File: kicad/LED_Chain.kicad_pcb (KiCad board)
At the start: 2 copper layers, 66.7 x 31.5 mm, 32 parts, among them J1 Interface, J2 PWR, J3 NeoPixel R1 A, J4 NeoPixel R1 B, J5 NeoPixel R1 C, J6 NeoPixel R1 D, J7 L1, J8 L2, Q1 IRLML2502, Q2 IRLML2502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

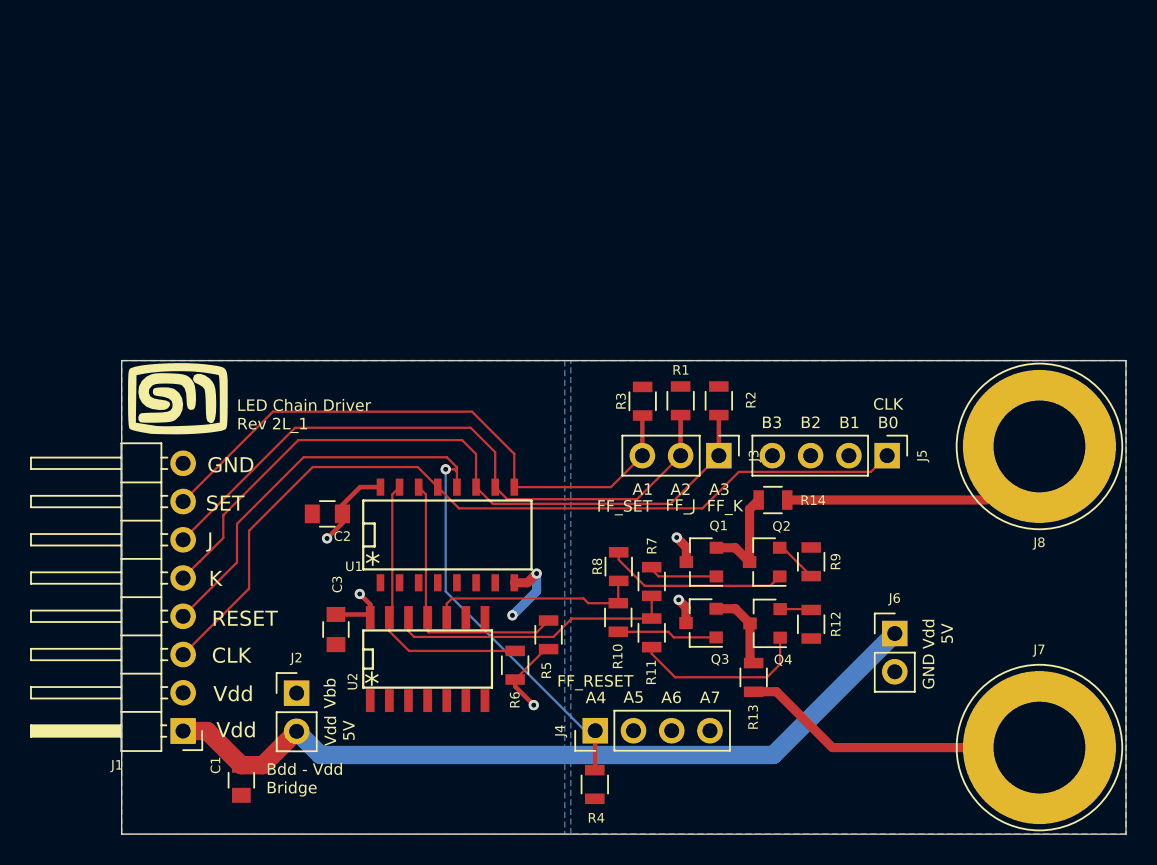
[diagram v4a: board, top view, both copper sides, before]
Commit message: Completed layout and sent to OSH Park
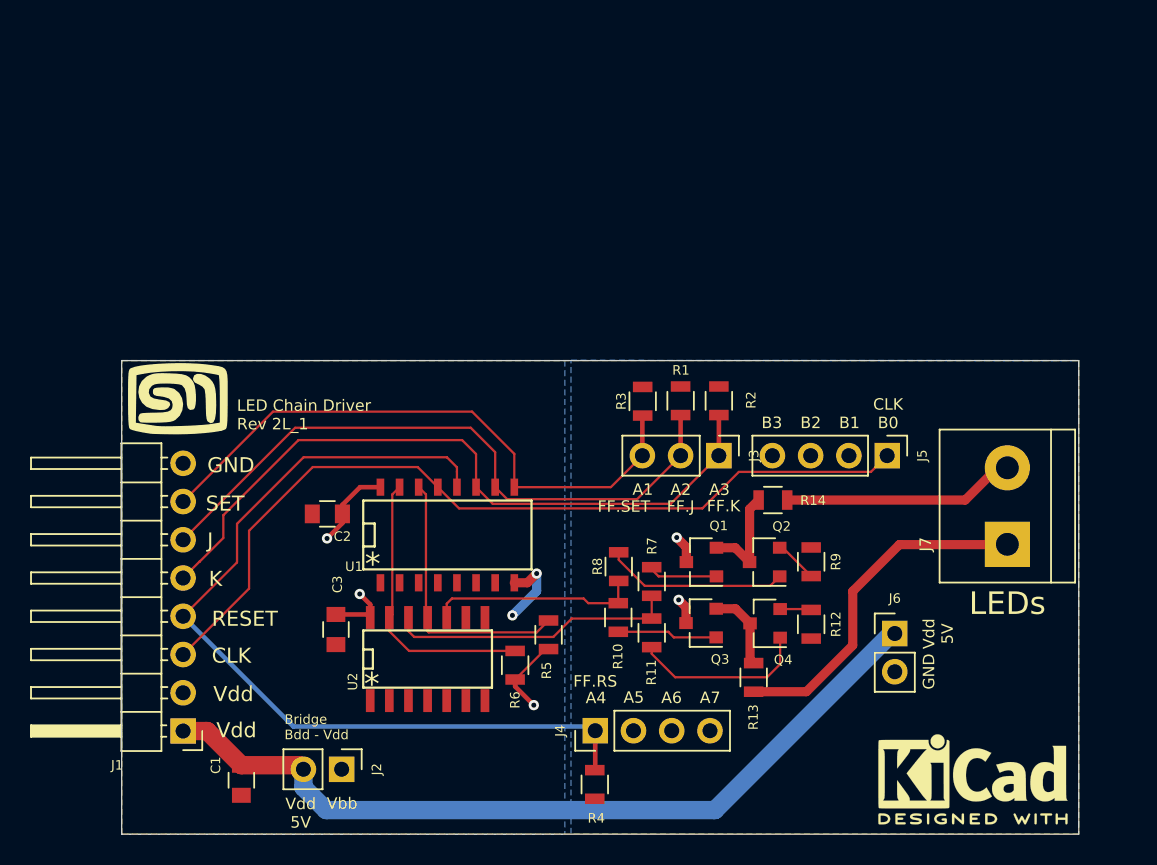
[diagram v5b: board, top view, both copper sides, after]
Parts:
- removed J8: L2, Connect:Banana_Jack_1Pin
- added G***: LOGO, LED_Chain:MyBasic_rounded_50_1, B.Cu at (149.7, 94.3)
- added REF***: KiCad-Logo2_6mm_SilkScreen, Symbols:KiCad-Logo2_6mm_SilkScreen, B.Cu at (173.1, 107.8)
- added REF***: KiCad-Logo2_6mm_SilkScreen, Symbols:KiCad-Logo2_6mm_SilkScreen, F.Cu at (173.1, 107.7)
- J7: value L1 -> LED; footprint Connect:Banana_Jack_1Pin -> LED_Chain:TerminalBlock_bornier-2_P5.08mm
- moved J7 13.7 mm to (175.4, 92.1), turned to 90 degrees
- moved J2 5.88 mm to (131.2, 107.1), turned to 270 degrees
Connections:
- net Net-(J7-Pad1) renamed /LED1
- R14 pad 1: Net-(J8-Pad1) -> /LED2
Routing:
- net Net-(J8-Pad1): track 18.2 -> 0.00 mm
- net /LED2: track 0.00 -> 14.8 mm
- net /A4: track 51.0 -> 58.8 mm, vias 1 -> 0
- net /5V: track 56.8 -> 58.9 mm
- net /LED1: track 21.7 -> 23.5 mm
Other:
- board size 66.7 x 31.5 mm -> 63.6 x 31.5 mm
- board text added: "Bridge Bdd - Vdd"
- board text added: "FF.J"
- board text added: "FF.K"
- board text added: "FF.RS"
- board text added: "FF.SET"
- board text added: "LEDs"
- board text removed: "B0 CLK"
- board text removed: "Bdd - Vdd Bridge"
- board text removed: "FF_J"
- board text removed: "FF_K"
- board text removed: "FF_RESET"
- board text removed: "FF_SET"

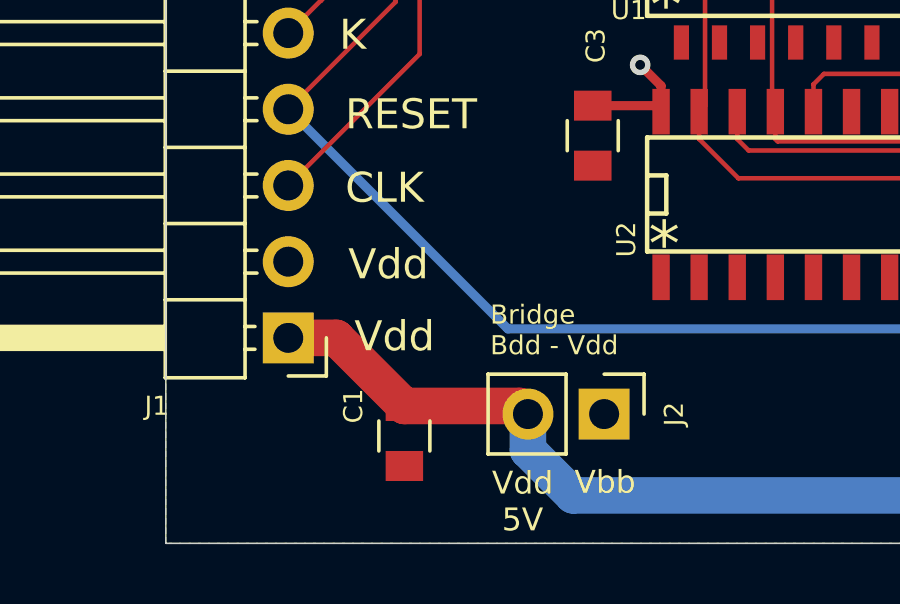
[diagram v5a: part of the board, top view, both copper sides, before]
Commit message: Makes a small correction to the labelling of the Vbb-Vdd bridge
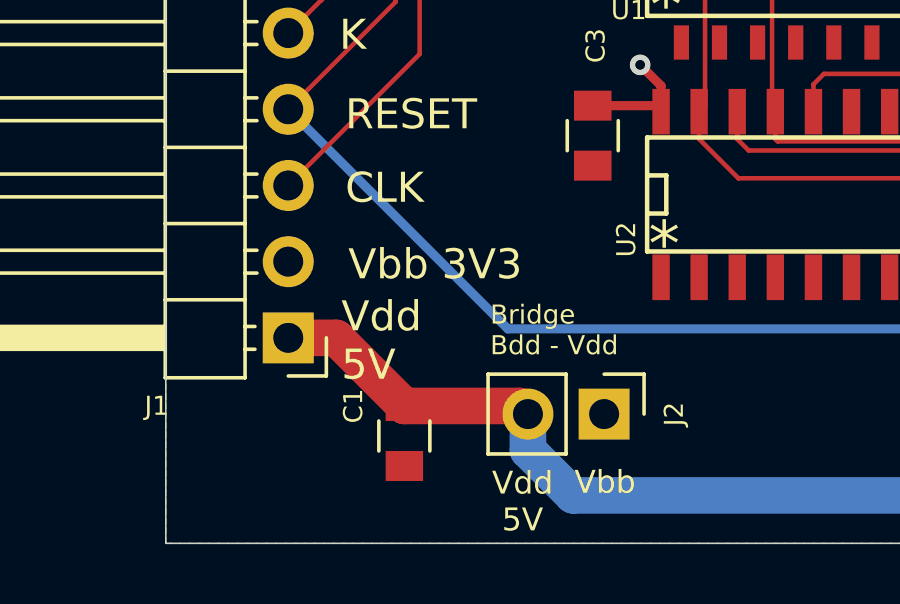
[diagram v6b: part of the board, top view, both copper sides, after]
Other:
- board text added: "Vbb 3V3"
- board text removed: "Vdd"
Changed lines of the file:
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@@
   )
   (setup
-    (last_trace_width 0.3048)
+    (last_trace_width 0.1524)
     (user_trace_width 0.3048)
     (user_trace_width 0.6096)
@@
       (effects (font (size 1 1) (thickness 0.15)))
     )
-    (fp_text user %R (at 2.54 0 90) (layer F.Fab)
-      (effects (font (size 1 1) (thickness 0.15)))
-    )
     (fp_line (start -2.41 2.85) (end 7.49 2.85) (layer F.Fab) (width 0.1))
     (fp_line (start -2.46 -4.45) (end -2.46 4.45) (layer F.Fab) (width 0.1))
@@
     (fp_line (start 7.79 4.7) (end 7.79 -4.7) (layer F.CrtYd) (width 0.05))
     (fp_line (start 7.79 4.7) (end -2.71 4.7) (layer F.CrtYd) (width 0.05))
+    (fp_text user %R (at 2.54 0 90) (layer F.Fab)
+      (effects (font (size 1 1) (thickness 0.15)))
+    )
     (pad 1 thru_hole rect (at 0 0 90) (size 3 3) (drill 1.52) (layers *.Cu *.Mask)
       (net 21 /LED1))
@@
   (gr_line (start 157.37 106.34) (end 107.61 106.34) (layer Dwgs.User) (width 0.15))
   (gr_line (start 149.36 80.62) (end 149.36 110.62) (layer Dwgs.User) (width 0.15))
-  (gr_text Vdd (at 125.513333 104.47) (layer F.SilkS)
-    (effects (font (size 1 1) (thickness 0.15)) (justify right))
-  )
-  (gr_text Vdd (at 122.660951 104.470001) (layer B.SilkS)
+  (gr_text "Vdd \n5V" (at 122.4 104.61) (layer F.SilkS)
+    (effects (font (size 1 1) (thickness 0.15)) (justify left))
+  )
+  (gr_text "Vdd 5V" (at 122.660951 104.470001) (layer B.SilkS)
     (effects (font (size 1 1) (thickness 0.15)) (justify right mirror))
   )
@@
     (effects (font (size 1 1) (thickness 0.15)) (justify right mirror))
   )
-  (gr_text Vdd (at 122.66095 102.070001) (layer B.SilkS)
+  (gr_text "Vbb 3V3" (at 122.66095 102.070001) (layer B.SilkS)
     (effects (font (size 1 1) (thickness 0.15)) (justify right mirror))
   )
-  (gr_text Vdd (at 122.63 102.07) (layer F.SilkS)
+  (gr_text "Vbb 3V3" (at 122.63 102.07) (layer F.SilkS)
     (effects (font (size 1 1) (thickness 0.15)) (justify left))
   )
@@
   (segment (start 134.326999 97.892399) (end 135.6346 99.2) (width 0.1524) (layer F.Cu) (net 14))
   (segment (start 134.326999 96.979999) (end 134.326999 97.892399) (width 0.1524) (layer F.Cu) (net 14))
-  (segment (start 158.52 101.91) (end 159.67 101.91) (width 0.1524) (layer F.Cu) (net 21))
   (via (at 153.54 95.81) (size 0.6858) (drill 0.3302) (layers F.Cu B.Cu) (net 15))
   (segment (start 154.03 96.3) (end 153.54 95.81) (width 0.6096) (layer F.Cu) (net 15))
@@
   (segment (start 140.084999 86.124999) (end 140.084999 88.324998) (width 0.1524) (layer F.Cu) (net 20))
   (segment (start 139.16 85.2) (end 140.084999 86.124999) (width 0.1524) (layer F.Cu) (net 20))
+  (segment (start 158.52 101.91) (end 159.67 101.91) (width 0.1524) (layer F.Cu) (net 21))
   (segment (start 168.2 92.14) (end 174.69 92.14) (width 0.6096) (layer F.Cu) (net 21))
   (segment (start 165.1 95.24) (end 168.2 92.14) (width 0.6096) (layer F.Cu) (net 21))

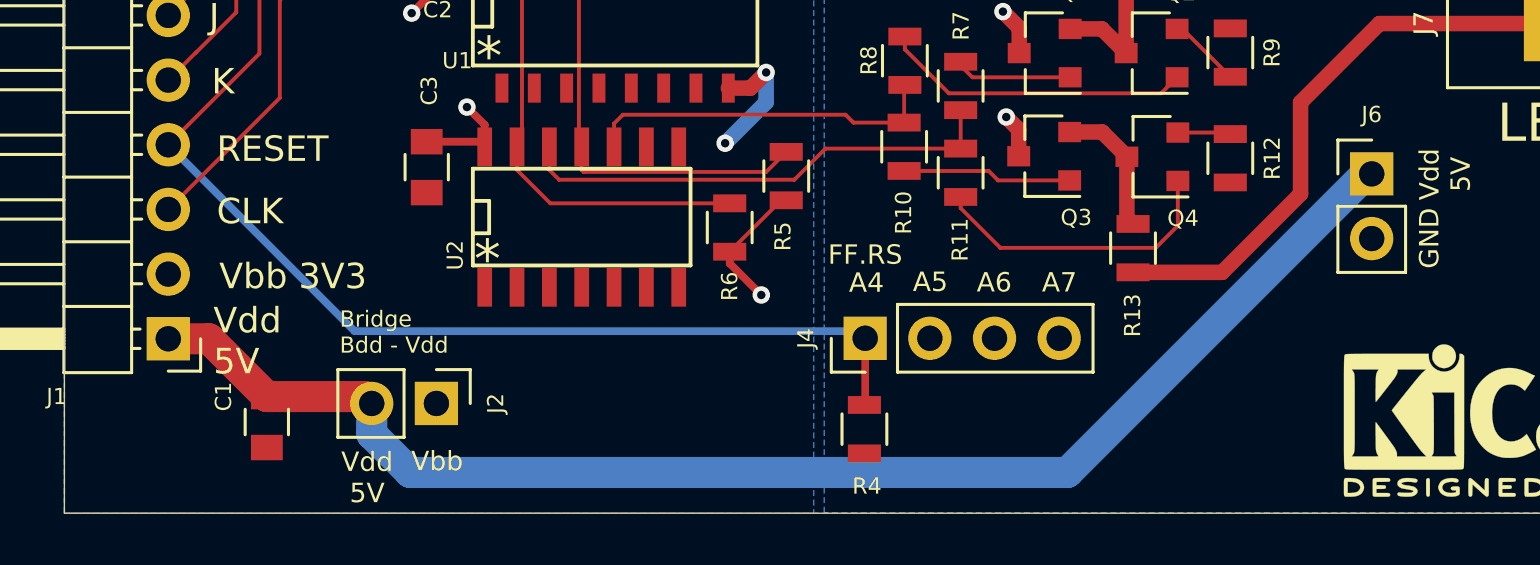
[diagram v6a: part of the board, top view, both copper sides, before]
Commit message: Makes a small correction to the labelling of the Vbb-Vdd bridge
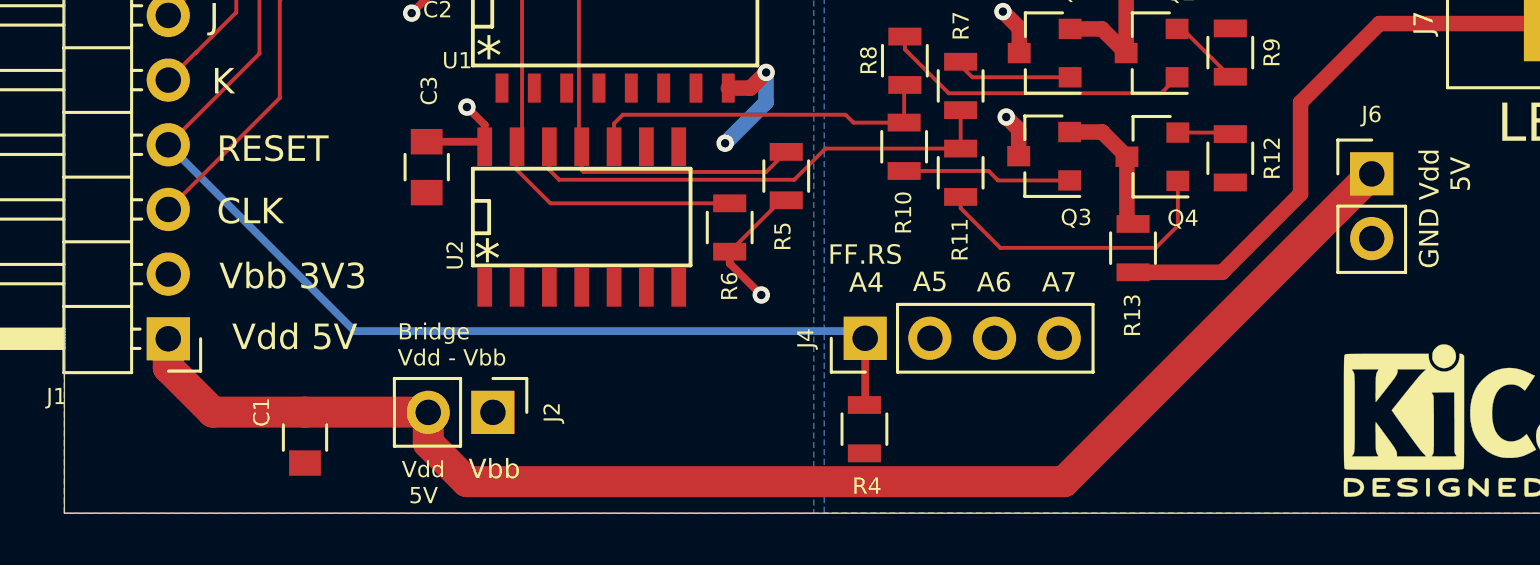
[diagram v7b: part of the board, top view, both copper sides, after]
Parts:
- moved J2 2.25 mm to (133.4, 107.4)
- moved C1 1.62 mm to (126.0, 108.4)
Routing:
- net /5V: track 58.9 -> 59.6 mm
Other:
- board text added: "Bridge Vdd - Vbb"
- board text removed: "Bridge Bdd - Vdd"
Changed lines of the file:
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@@
   )
   (setup
-    (last_trace_width 0.1524)
+    (last_trace_width 1.2192)
     (user_trace_width 0.3048)
     (user_trace_width 0.6096)
@@
   )
   (module Pin_Headers:Pin_Header_Straight_1x02_Pitch2.54mm (layer F.Cu)
-    (at 131.16 107.06 270)
+    (at 133.38 107.41 270)
     (descr "Through hole straight pin header, 1x02, 2.54mm pitch, single row")
     (tags "Through hole pin header THT 1x02 2.54mm single row")
@@
   )
   (module Capacitors_SMD:C_0805 (layer F.Cu)
-    (at 124.5 107.79 270)
+    (at 126 108.4 270)
     (descr "Capacitor SMD 0805, reflow soldering, AVX (see smccp.pdf)")
     (tags "capacitor 0805")
@@
     (effects (font (size 1.524 1.524) (thickness 0.127)) (justify left))
   )
-  (gr_text Vbb (at 131.19 109.33) (layer F.SilkS)
+  (gr_text Vbb (at 133.44 109.64) (layer F.SilkS)
     (effects (font (size 0.762 0.762) (thickness 0.127)))
   )
-  (gr_text "Vdd\n5V" (at 128.44 109.97) (layer F.SilkS)
-    (effects (font (size 0.762 0.762) (thickness 0.127)))
+  (gr_text "Vdd\n5V" (at 130.65 110.17) (layer F.SilkS)
+    (effects (font (size 0.635 0.635) (thickness 0.127)))
   )
   (gr_text FF.K (at 155.41 89.58) (layer F.SilkS)
@@
     (effects (font (size 0.762 0.762) (thickness 0.127)))
   )
-  (gr_text "Bridge\nBdd - Vdd" (at 127.36 104.26) (layer F.SilkS)
+  (gr_text "Bridge\nVdd - Vbb" (at 129.64 104.76) (layer F.SilkS)
     (effects (font (size 0.635 0.635) (thickness 0.127)) (justify left))
   )
@@
   (gr_line (start 157.37 106.34) (end 107.61 106.34) (layer Dwgs.User) (width 0.15))
   (gr_line (start 149.36 80.62) (end 149.36 110.62) (layer Dwgs.User) (width 0.15))
-  (gr_text "Vdd \n5V" (at 122.4 104.61) (layer F.SilkS)
-    (effects (font (size 1 1) (thickness 0.15)) (justify left))
+  (gr_text "Vdd 5V" (at 128.06 104.46) (layer F.SilkS)
+    (effects (font (size 1 1) (thickness 0.15)) (justify right))
   )
   (gr_text "Vdd 5V" (at 122.660951 104.470001) (layer B.SilkS)
@@
   (segment (start 154.049999 92.309999) (end 153.41 91.67) (width 0.6096) (layer F.Cu) (net 15))
   (segment (start 154.049999 93.299999) (end 154.049999 92.309999) (width 0.6096) (layer F.Cu) (net 15))
-  (segment (start 122.23 104.52) (end 124.5 106.79) (width 1.2192) (layer F.Cu) (net 15))
-  (segment (start 120.63 104.52) (end 122.23 104.52) (width 1.2192) (layer F.Cu) (net 15))
-  (segment (start 128.35 106.79) (end 128.62 107.06) (width 1.2192) (layer F.Cu) (net 15))
-  (segment (start 124.5 106.79) (end 128.35 106.79) (width 1.2192) (layer F.Cu) (net 15))
-  (segment (start 167.894 98.044) (end 167.894 97.824) (width 1.2192) (layer B.Cu) (net 15))
-  (segment (start 167.894 97.824) (end 155.948 109.77) (width 1.2192) (layer B.Cu) (net 15))
-  (segment (start 128.62 108.262081) (end 128.62 107.06) (width 1.2192) (layer B.Cu) (net 15))
-  (segment (start 130.127919 109.77) (end 128.62 108.262081) (width 1.2192) (layer B.Cu) (net 15))
-  (segment (start 155.948 109.77) (end 130.127919 109.77) (width 1.2192) (layer B.Cu) (net 15))
+  (segment (start 120.63 104.52) (end 120.63 105.65) (width 1.2192) (layer F.Cu) (net 15))
+  (segment (start 122.38 107.4) (end 126 107.4) (width 1.2192) (layer F.Cu) (net 15))
+  (segment (start 120.63 105.65) (end 122.38 107.4) (width 1.2192) (layer F.Cu) (net 15))
+  (segment (start 130.83 107.4) (end 130.84 107.41) (width 1.2192) (layer F.Cu) (net 15))
+  (segment (start 126 107.4) (end 130.83 107.4) (width 1.2192) (layer F.Cu) (net 15))
+  (segment (start 130.84 108.612081) (end 132.35992 110.132001) (width 1.2192) (layer F.Cu) (net 15))
+  (segment (start 130.84 107.41) (end 130.84 108.612081) (width 1.2192) (layer F.Cu) (net 15))
+  (segment (start 155.805999 110.132001) (end 167.894 98.044) (width 1.2192) (layer F.Cu) (net 15))
+  (segment (start 132.35992 110.132001) (end 155.805999 110.132001) (width 1.2192) (layer F.Cu) (net 15))
   (segment (start 138.954721 89.734719) (end 155.114719 89.734719) (width 0.1524) (layer F.Cu) (net 16))
   (segment (start 137.544999 88.324998) (end 138.954721 89.734719) (width 0.1524) (layer F.Cu) (net 16))

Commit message: Fixes the pin association on J3
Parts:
- moved R2 7.77 mm to (148.4, 82.2), turned to 0 degrees
- moved R3 4.44 mm to (155.6, 82.2), turned to 0 degrees
- moved R1 1.76 mm to (151.9, 82.2), turned to 0 degrees
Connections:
- J3 pad 1: /A3 -> /A1
- J3 pad 3: /A1 -> /A3
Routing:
- net /A1: track 39.9 -> 49.0 mm, vias 0 -> 1
- net /A2: track 43.3 -> 45.9 mm
- net /A3: track 47.3 -> 44.8 mm, vias 0 -> 1
